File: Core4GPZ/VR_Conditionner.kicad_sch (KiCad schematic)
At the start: 16 parts, among them U4 MAX9926UAEE+

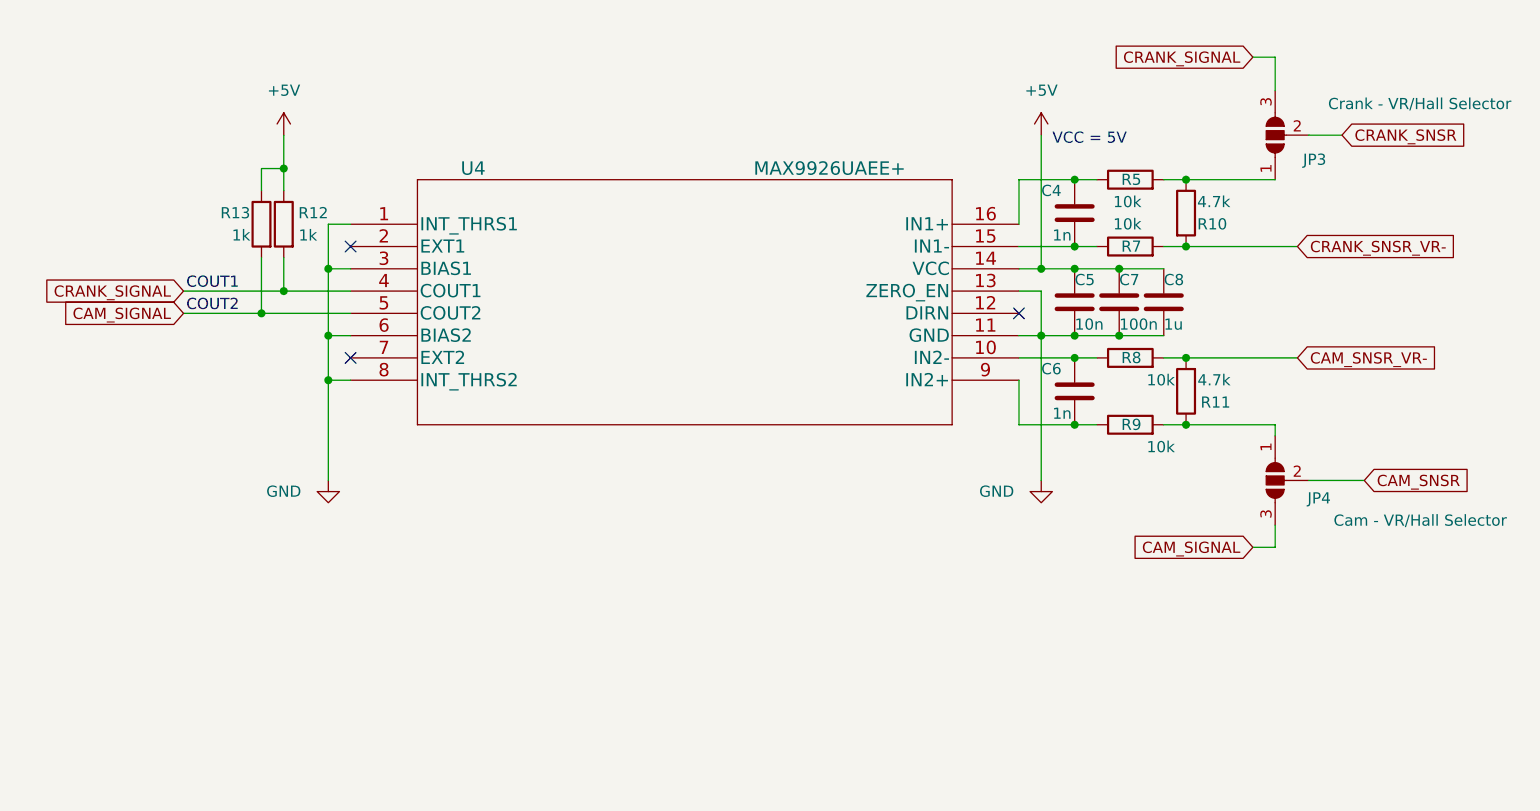
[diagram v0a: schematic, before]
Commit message: Started Implementation of VR Conditionner
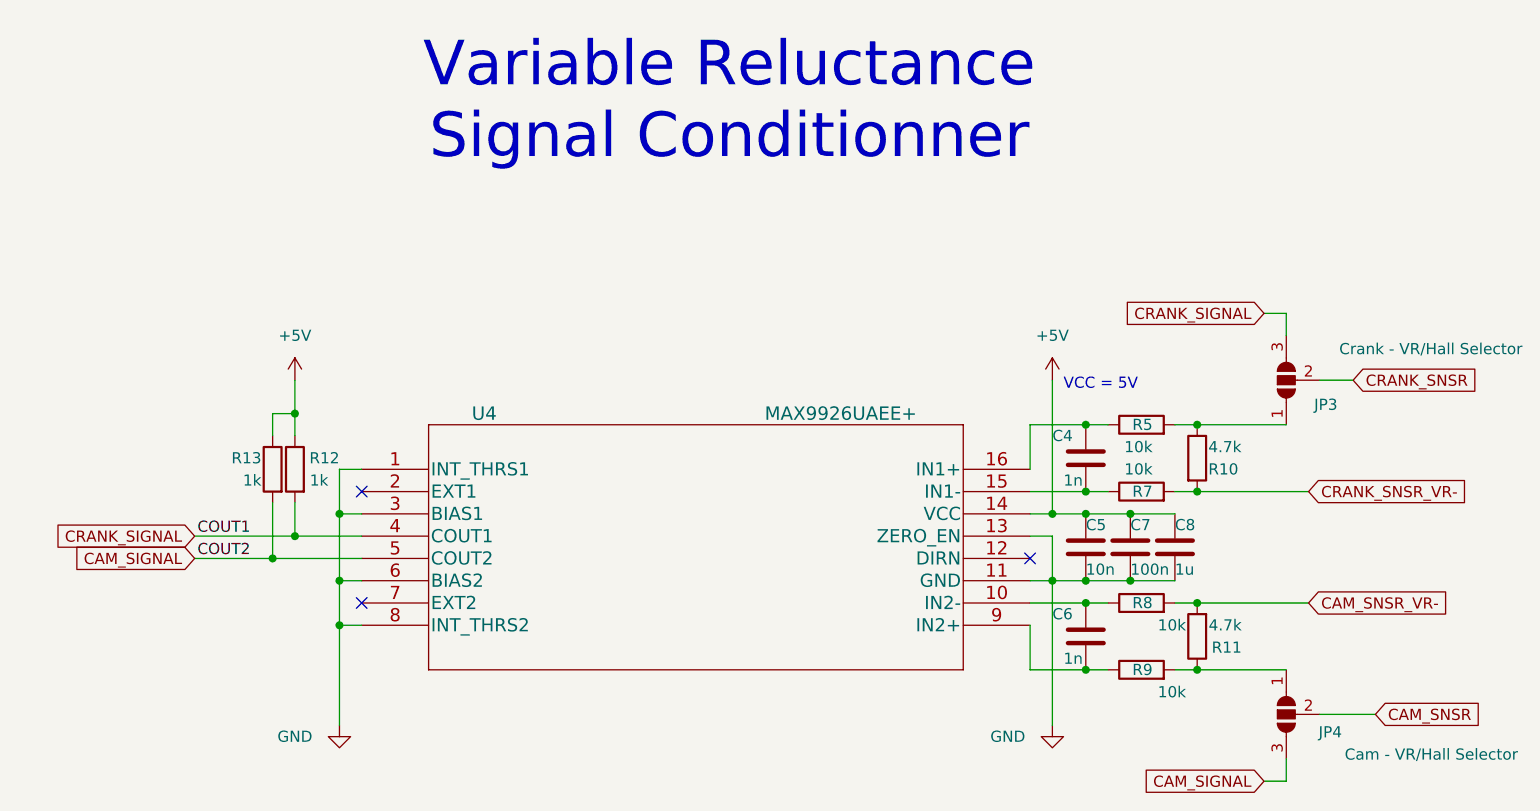
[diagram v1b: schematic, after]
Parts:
- R12, R13: footprint Resistor_SMD:R_0603_1608Metric_Pad1.05x0.95mm_HandSolder -> Resistor_SMD:R_0603_1608Metric_Pad0.98x0.95mm_HandSolder
- R5, R7, R8, R9: footprint Resistor_SMD:R_1206_3216Metric -> Resistor_SMD:R_1206_3216Metric_Pad1.30x1.75mm_HandSolder
- U4: footprint MAX9926UAEE+:MAX9926UAEE&plus_ -> Package_SO:QSOP-16_3.9x4.9mm_P0.635mm
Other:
- note added: "Variable Reluctance Signal Conditionner"
- moved on the sheet: C4, C5, C6, C7, C8, JP3, JP4, R10, R11, R12, R13, R5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

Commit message: Implemented VR_Conditionner (MAX9926+)
First look at ground plane
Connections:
- net CRANK_SIGNAL: now also JP3.1 (A); no longer JP3.3 (B)
- net at R10.1, R5.2: now also JP3.3 (B); no longer JP3.1 (A)
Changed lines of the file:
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@@
 		(lib_id "Jumper:SolderJumper_3_Open")
 		(at 205.74 66.04 90)
+		(mirror x)
 		(unit 1)
 		(exclude_from_sim yes)
@@
 		(dnp no)
 		(property "Reference" "JP3"
-			(at 211.582 68.834 90)
+			(at 211.582 63.246 90)
 			(effects
 				(font
@@
 		)
 		(property "Value" "Crank - VR/Hall Selector"
-			(at 232.664 62.484 90)
+			(at 232.664 69.596 90)
 			(effects
 				(font
